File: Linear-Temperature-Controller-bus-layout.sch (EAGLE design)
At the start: 78 parts, among them IC1 LM393D, IC3 AD5624R, IC4 AD5262, IC5 LF356MX, T1 MMBT3904, T2 MMBT3904

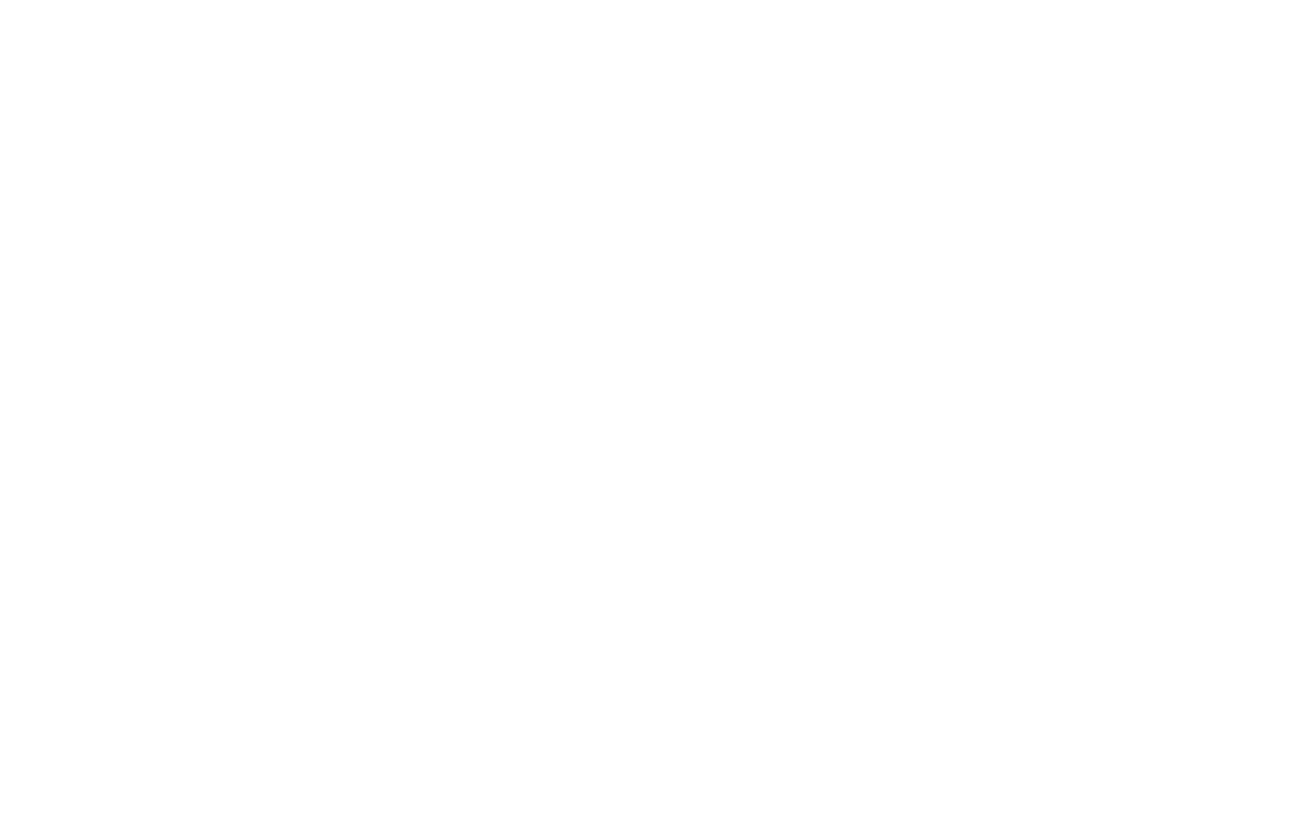
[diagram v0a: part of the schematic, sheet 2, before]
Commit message: Finished first attempt at board layout
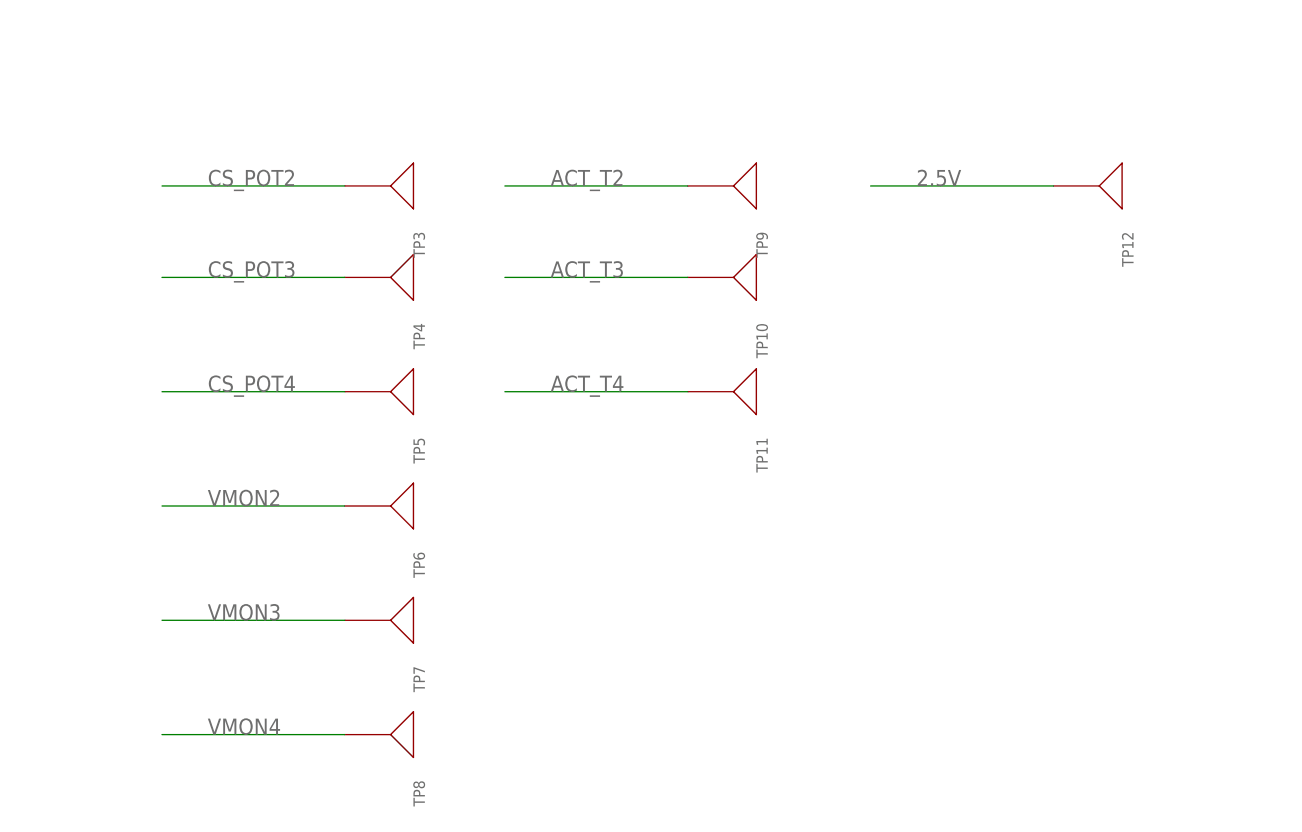
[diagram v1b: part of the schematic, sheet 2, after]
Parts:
- added TP10, TP11, TP12, TP3, TP4, TP5, TP6, TP7, TP8, TP9: TESTPT, Lin-Temp-Controller:TESTPT
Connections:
- net 2.5V: now also TP12.P$1
- net ACT_T2: now also TP9.P$1
- net ACT_T3: now also TP10.P$1
- net ACT_T4: now also TP11.P$1
- net CS_POT2: now also TP3.P$1
- net CS_POT3: now also TP4.P$1
- net CS_POT4: now also TP5.P$1
- net VMON2: now also TP6.P$1
- net VMON3: now also TP7.P$1
- net VMON4: now also TP8.P$1
